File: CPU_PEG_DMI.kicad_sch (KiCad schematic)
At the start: 1 part

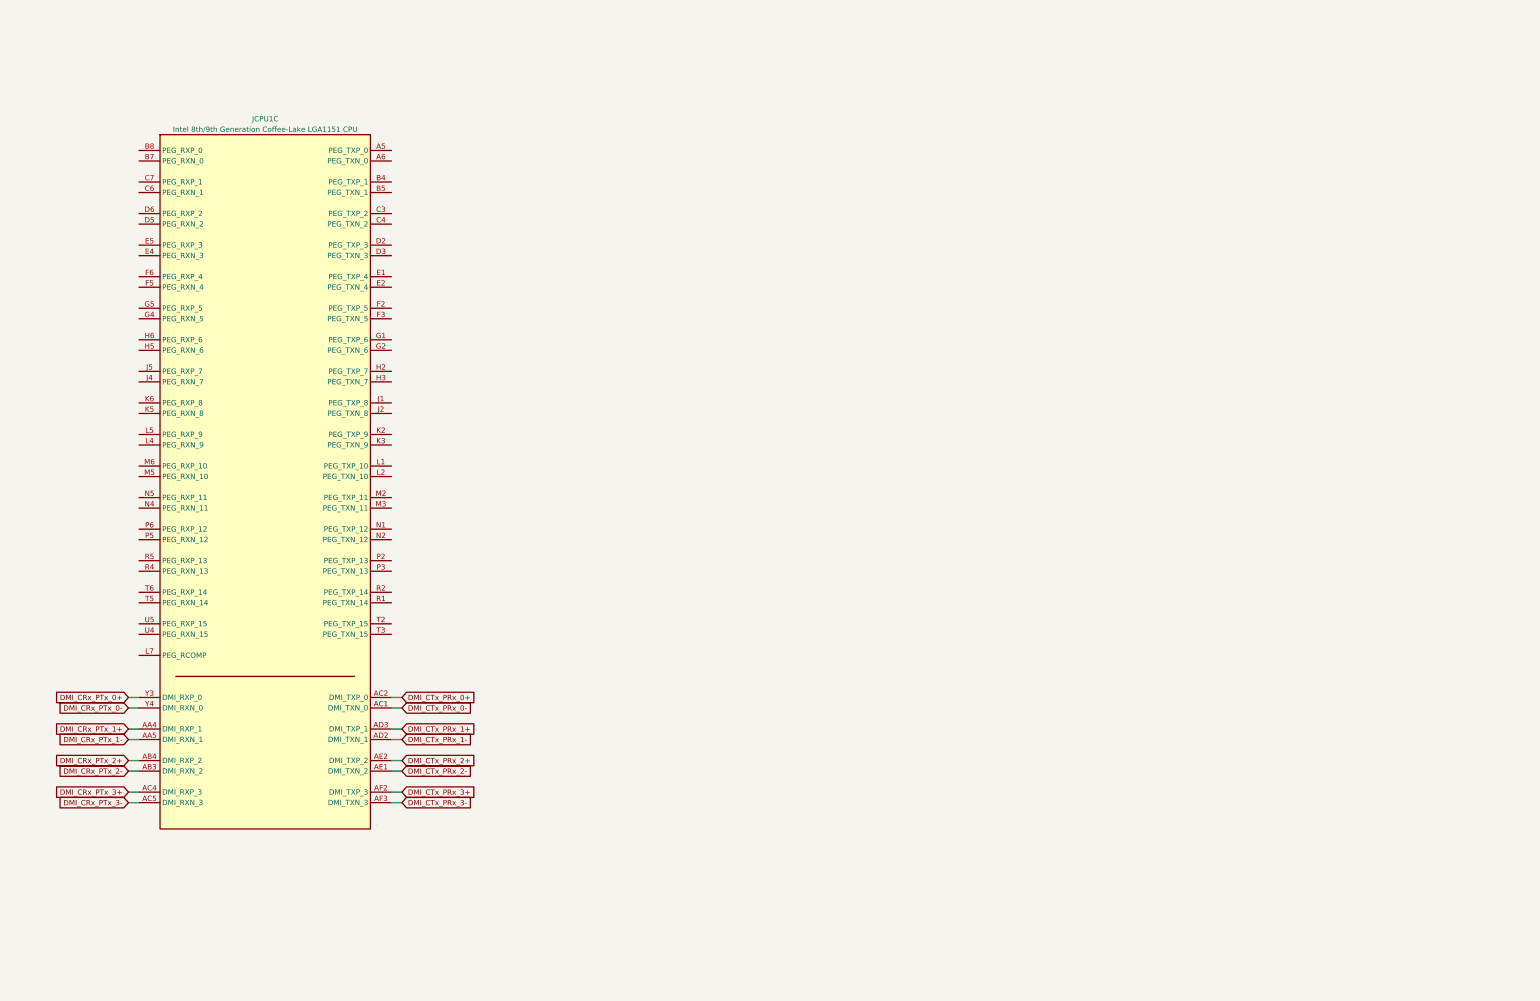
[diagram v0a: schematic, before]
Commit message: Added PCIe x16 slot
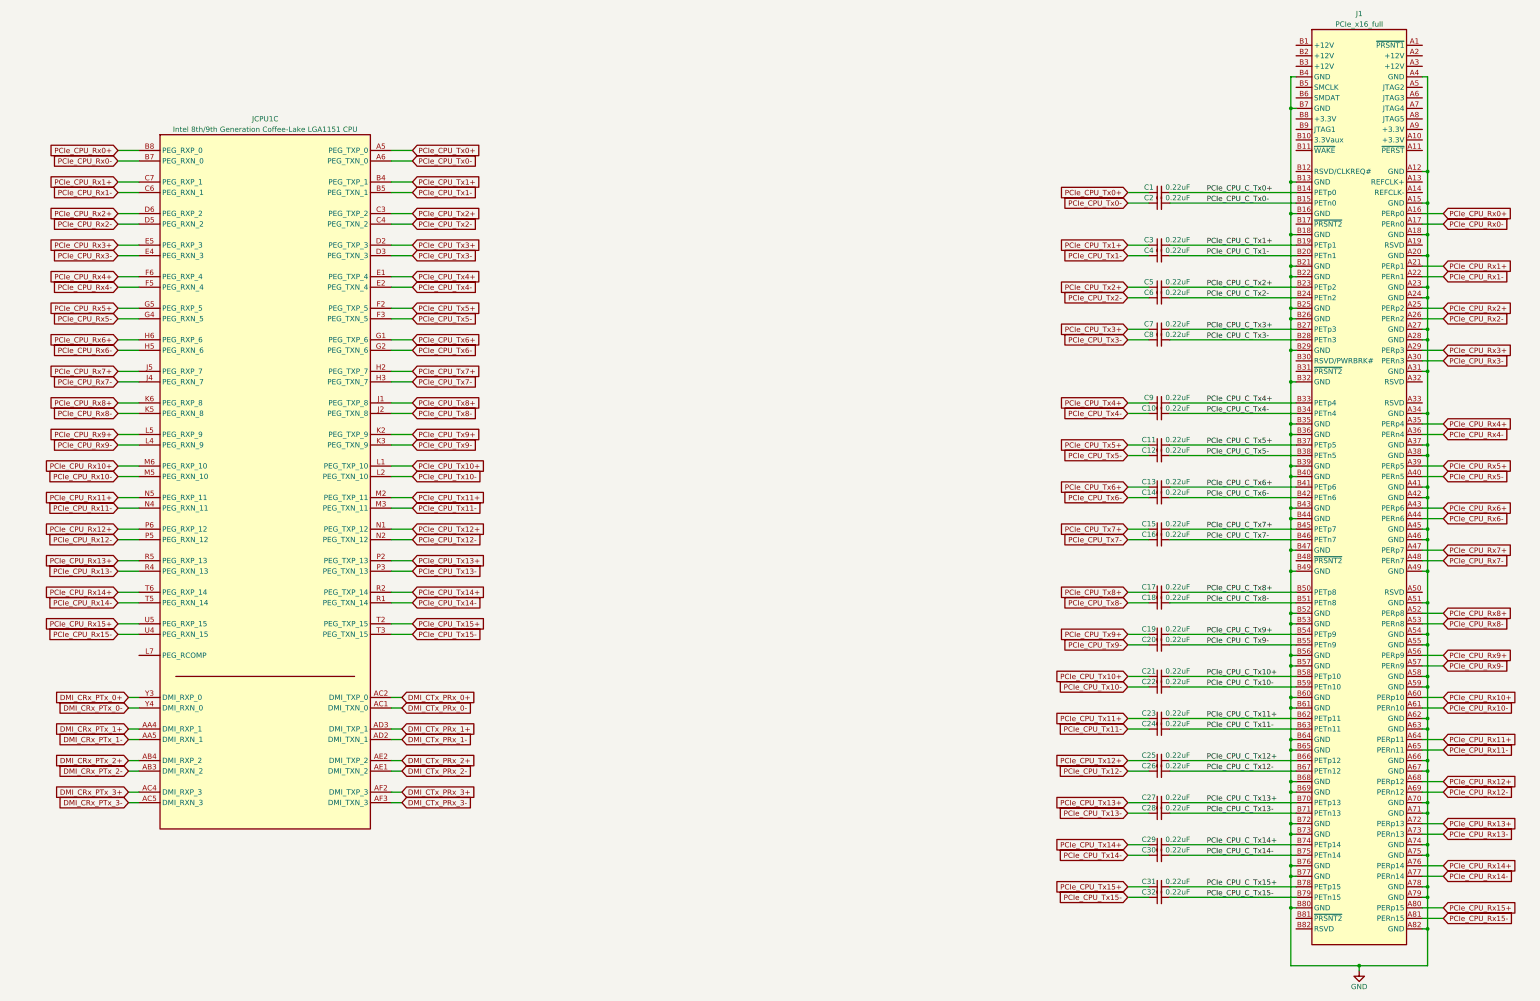
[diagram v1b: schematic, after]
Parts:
- added C1, C10, C11, C12, C13, C14, C15, C16, C17, C18, C19, C2, C20, C21, C22, C23, C24, C25, C26, C27, C28, C29, C3, C30, C31, C32, C4, C5, C6, C7, C8, C9: 0.22uF, Capacitor_SMD:C_0402_1005Metric, symbol Device:C_Small
- added J1: PCIe_x16_full, A-my-stuff:PCIe_x16_tht_smallholes, symbol A-my-stuff:PCIe_x16_full
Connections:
- net PCIe_CPU_Tx0+: now reaches JCPU1.A5 (PEG_TXP_0)
- net PCIe_CPU_Tx0+: now also C1.1
- net PCIe_CPU_Tx0-: now reaches JCPU1.A6 (PEG_TXN_0)
- net PCIe_CPU_Tx0-: now also C2.1
- net PCIe_CPU_Tx1+: now reaches JCPU1.B4 (PEG_TXP_1)
- net PCIe_CPU_Tx1+: now also C3.1
- net PCIe_CPU_Tx1-: now reaches JCPU1.B5 (PEG_TXN_1)
- net PCIe_CPU_Tx1-: now also C4.1
- net PCIe_CPU_Rx0-: now reaches JCPU1.B7 (PEG_RXN_0)
- net PCIe_CPU_Rx0-: now also J1.A17 (PERn0)
- net PCIe_CPU_Rx0+: now reaches JCPU1.B8 (PEG_RXP_0)
- net PCIe_CPU_Rx0+: now also J1.A16 (PERp0)
- net PCIe_CPU_Tx2+: now reaches JCPU1.C3 (PEG_TXP_2)
- net PCIe_CPU_Tx2+: now also C5.1
- net PCIe_CPU_Tx2-: now reaches JCPU1.C4 (PEG_TXN_2)
- net PCIe_CPU_Tx2-: now also C6.1
- net PCIe_CPU_Rx1-: now reaches JCPU1.C6 (PEG_RXN_1)
- net PCIe_CPU_Rx1-: now also J1.A22 (PERn1)
- net PCIe_CPU_Rx1+: now reaches JCPU1.C7 (PEG_RXP_1)
- net PCIe_CPU_Rx1+: now also J1.A21 (PERp1)
- net PCIe_CPU_Tx3+: now reaches JCPU1.D2 (PEG_TXP_3)
- net PCIe_CPU_Tx3+: now also C7.1
- net PCIe_CPU_Tx3-: now reaches JCPU1.D3 (PEG_TXN_3)
- net PCIe_CPU_Tx3-: now also C8.1
- net PCIe_CPU_Rx2-: now reaches JCPU1.D5 (PEG_RXN_2)
- net PCIe_CPU_Rx2-: now also J1.A26 (PERn2)
- net PCIe_CPU_Rx2+: now reaches JCPU1.D6 (PEG_RXP_2)
- net PCIe_CPU_Rx2+: now also J1.A25 (PERp2)
- net PCIe_CPU_Tx4+: now reaches JCPU1.E1 (PEG_TXP_4)
- net PCIe_CPU_Tx4+: now also C9.1
- net PCIe_CPU_Tx4-: now reaches JCPU1.E2 (PEG_TXN_4)
- net PCIe_CPU_Tx4-: now also C10.1
- net PCIe_CPU_Rx3-: now reaches JCPU1.E4 (PEG_RXN_3)
- net PCIe_CPU_Rx3-: now also J1.A30 (PERn3)
- net PCIe_CPU_Rx3+: now reaches JCPU1.E5 (PEG_RXP_3)
- net PCIe_CPU_Rx3+: now also J1.A29 (PERp3)
- net PCIe_CPU_Tx5+: now reaches JCPU1.F2 (PEG_TXP_5)
- net PCIe_CPU_Tx5+: now also C11.1
- net PCIe_CPU_Tx5-: now reaches JCPU1.F3 (PEG_TXN_5)
- net PCIe_CPU_Tx5-: now also C12.1
- net PCIe_CPU_Rx4-: now reaches JCPU1.F5 (PEG_RXN_4)
- net PCIe_CPU_Rx4-: now also J1.A36 (PERn4)
- net PCIe_CPU_Rx4+: now reaches JCPU1.F6 (PEG_RXP_4)
- net PCIe_CPU_Rx4+: now also J1.A35 (PERp4)
- net PCIe_CPU_Tx6+: now reaches JCPU1.G1 (PEG_TXP_6)
- net PCIe_CPU_Tx6+: now also C13.1
- net PCIe_CPU_Tx6-: now reaches JCPU1.G2 (PEG_TXN_6)
- net PCIe_CPU_Tx6-: now also C14.1
- net PCIe_CPU_Rx5-: now reaches JCPU1.G4 (PEG_RXN_5)
- net PCIe_CPU_Rx5-: now also J1.A40 (PERn5)
- net PCIe_CPU_Rx5+: now reaches JCPU1.G5 (PEG_RXP_5)
- net PCIe_CPU_Rx5+: now also J1.A39 (PERp5)
- net PCIe_CPU_Tx7+: now reaches JCPU1.H2 (PEG_TXP_7)
- net PCIe_CPU_Tx7+: now also C15.1
- net PCIe_CPU_Tx7-: now reaches JCPU1.H3 (PEG_TXN_7)
- net PCIe_CPU_Tx7-: now also C16.1
- net PCIe_CPU_Rx6-: now reaches JCPU1.H5 (PEG_RXN_6)
- net PCIe_CPU_Rx6-: now also J1.A44 (PERn6)
- net PCIe_CPU_Rx6+: now reaches JCPU1.H6 (PEG_RXP_6)
- net PCIe_CPU_Rx6+: now also J1.A43 (PERp6)
- net PCIe_CPU_Tx8+: now reaches JCPU1.J1 (PEG_TXP_8)
- net PCIe_CPU_Tx8+: now also C17.1
- net PCIe_CPU_Tx8-: now reaches JCPU1.J2 (PEG_TXN_8)
- net PCIe_CPU_Tx8-: now also C18.1
- net PCIe_CPU_Rx7-: now reaches JCPU1.J4 (PEG_RXN_7)
- net PCIe_CPU_Rx7-: now also J1.A48 (PERn7)
- net PCIe_CPU_Rx7+: now reaches JCPU1.J5 (PEG_RXP_7)
- net PCIe_CPU_Rx7+: now also J1.A47 (PERp7)
- net PCIe_CPU_Tx9+: now reaches JCPU1.K2 (PEG_TXP_9)
- net PCIe_CPU_Tx9+: now also C19.1
- net PCIe_CPU_Tx9-: now reaches JCPU1.K3 (PEG_TXN_9)
- net PCIe_CPU_Tx9-: now also C20.1
- net PCIe_CPU_Rx8-: now reaches JCPU1.K5 (PEG_RXN_8)
- net PCIe_CPU_Rx8-: now also J1.A53 (PERn8)
- net PCIe_CPU_Rx8+: now reaches JCPU1.K6 (PEG_RXP_8)
- net PCIe_CPU_Rx8+: now also J1.A52 (PERp8)
- net PCIe_CPU_Tx10+: now reaches JCPU1.L1 (PEG_TXP_10)
- net PCIe_CPU_Tx10+: now also C21.1
- net PCIe_CPU_Tx10-: now reaches JCPU1.L2 (PEG_TXN_10)
- net PCIe_CPU_Tx10-: now also C22.1
- net PCIe_CPU_Rx9-: now reaches JCPU1.L4 (PEG_RXN_9)
- net PCIe_CPU_Rx9-: now also J1.A57 (PERn9)
- net PCIe_CPU_Rx9+: now reaches JCPU1.L5 (PEG_RXP_9)
- net PCIe_CPU_Rx9+: now also J1.A56 (PERp9)
- net PCIe_CPU_Tx11+: now reaches JCPU1.M2 (PEG_TXP_11)
- net PCIe_CPU_Tx11+: now also C23.1
- net PCIe_CPU_Tx11-: now reaches JCPU1.M3 (PEG_TXN_11)
- net PCIe_CPU_Tx11-: now also C24.1
- net PCIe_CPU_Rx10-: now reaches JCPU1.M5 (PEG_RXN_10)
- net PCIe_CPU_Rx10-: now also J1.A61 (PERn10)
- net PCIe_CPU_Rx10+: now reaches JCPU1.M6 (PEG_RXP_10)
- net PCIe_CPU_Rx10+: now also J1.A60 (PERp10)
- net PCIe_CPU_Tx12+: now reaches JCPU1.N1 (PEG_TXP_12)
- net PCIe_CPU_Tx12+: now also C25.1
- net PCIe_CPU_Tx12-: now reaches JCPU1.N2 (PEG_TXN_12)
- net PCIe_CPU_Tx12-: now also C26.1
- net PCIe_CPU_Rx11-: now reaches JCPU1.N4 (PEG_RXN_11)
- net PCIe_CPU_Rx11-: now also J1.A65 (PERn11)
- net PCIe_CPU_Rx11+: now reaches JCPU1.N5 (PEG_RXP_11)
- net PCIe_CPU_Rx11+: now also J1.A64 (PERp11)
- net PCIe_CPU_Tx13+: now reaches JCPU1.P2 (PEG_TXP_13)
- net PCIe_CPU_Tx13+: now also C27.1
- net PCIe_CPU_Tx13-: now reaches JCPU1.P3 (PEG_TXN_13)
- net PCIe_CPU_Tx13-: now also C28.1
- net PCIe_CPU_Rx12-: now reaches JCPU1.P5 (PEG_RXN_12)
- net PCIe_CPU_Rx12-: now also J1.A69 (PERn12)
- net PCIe_CPU_Rx12+: now reaches JCPU1.P6 (PEG_RXP_12)
- net PCIe_CPU_Rx12+: now also J1.A68 (PERp12)
- net PCIe_CPU_Tx14-: now reaches JCPU1.R1 (PEG_TXN_14)
- net PCIe_CPU_Tx14-: now also C30.1
- net PCIe_CPU_Tx14+: now reaches JCPU1.R2 (PEG_TXP_14)
- net PCIe_CPU_Tx14+: now also C29.1
- net PCIe_CPU_Rx13-: now reaches JCPU1.R4 (PEG_RXN_13)
- net PCIe_CPU_Rx13-: now also J1.A73 (PERn13)
- net PCIe_CPU_Rx13+: now reaches JCPU1.R5 (PEG_RXP_13)
- net PCIe_CPU_Rx13+: now also J1.A72 (PERp13)
- net PCIe_CPU_Tx15+: now reaches JCPU1.T2 (PEG_TXP_15)
- net PCIe_CPU_Tx15+: now also C31.1
- net PCIe_CPU_Tx15-: now reaches JCPU1.T3 (PEG_TXN_15)
- net PCIe_CPU_Tx15-: now also C32.1
- net PCIe_CPU_Rx14-: now reaches JCPU1.T5 (PEG_RXN_14)
- net PCIe_CPU_Rx14-: now also J1.A77 (PERn14)
- net PCIe_CPU_Rx14+: now reaches JCPU1.T6 (PEG_RXP_14)
- net PCIe_CPU_Rx14+: now also J1.A76 (PERp14)
- net PCIe_CPU_Rx15-: now reaches JCPU1.U4 (PEG_RXN_15)
- net PCIe_CPU_Rx15-: now also J1.A81 (PERn15)
- net PCIe_CPU_Rx15+: now reaches JCPU1.U5 (PEG_RXP_15)
- net PCIe_CPU_Rx15+: now also J1.A80 (PERp15)
- new net GND: J1.A12 (GND), J1.A15 (GND), J1.A18 (GND), J1.A20 (GND), J1.A23 (GND), J1.A24 (GND), J1.A27 (GND), J1.A28 (GND), J1.A31 (GND), J1.A34 (GND), J1.A37 (GND), J1.A38 (GND), J1.A4 (GND), J1.A41 (GND), J1.A42 (GND), J1.A45 (GND), J1.A46 (GND), J1.A49 (GND), J1.A51 (GND), J1.A54 (GND), J1.A55 (GND), J1.A58 (GND), J1.A59 (GND), J1.A62 (GND), J1.A63 (GND), J1.A66 (GND), J1.A67 (GND), J1.A70 (GND), J1.A71 (GND), J1.A74 (GND), J1.A75 (GND), J1.A78 (GND), J1.A79 (GND), J1.A82 (GND), J1.B13 (GND), J1.B16 (GND), J1.B18 (GND), J1.B21 (GND), J1.B22 (GND), J1.B25 (GND), J1.B26 (GND), J1.B29 (GND), J1.B32 (GND), J1.B35 (GND), J1.B36 (GND), J1.B39 (GND), J1.B4 (GND), J1.B40 (GND), J1.B43 (GND), J1.B44 (GND), J1.B47 (GND), J1.B49 (GND), J1.B52 (GND), J1.B53 (GND), J1.B56 (GND), J1.B57 (GND), J1.B60 (GND), J1.B61 (GND), J1.B64 (GND), J1.B65 (GND), J1.B68 (GND), J1.B69 (GND), J1.B7 (GND), J1.B72 (GND), J1.B73 (GND), J1.B76 (GND), J1.B77 (GND), J1.B80 (GND)
- new net PCIe_CPU_C_Tx0+: C1.2, J1.B14 (PETp0)
- new net PCIe_CPU_C_Tx0-: C2.2, J1.B15 (PETn0)
- new net PCIe_CPU_C_Tx1+: C3.2, J1.B19 (PETp1)
- new net PCIe_CPU_C_Tx1-: C4.2, J1.B20 (PETn1)
- new net PCIe_CPU_C_Tx10+: C21.2, J1.B58 (PETp10)
- new net PCIe_CPU_C_Tx10-: C22.2, J1.B59 (PETn10)
- new net PCIe_CPU_C_Tx11+: C23.2, J1.B62 (PETp11)
- new net PCIe_CPU_C_Tx11-: C24.2, J1.B63 (PETn11)
- new net PCIe_CPU_C_Tx12+: C25.2, J1.B66 (PETp12)
- new net PCIe_CPU_C_Tx12-: C26.2, J1.B67 (PETn12)
- new net PCIe_CPU_C_Tx13+: C27.2, J1.B70 (PETp13)
- new net PCIe_CPU_C_Tx13-: C28.2, J1.B71 (PETn13)
- new net PCIe_CPU_C_Tx14+: C29.2, J1.B74 (PETp14)
- new net PCIe_CPU_C_Tx14-: C30.2, J1.B75 (PETn14)
- new net PCIe_CPU_C_Tx15+: C31.2, J1.B78 (PETp15)
- new net PCIe_CPU_C_Tx15-: C32.2, J1.B79 (PETn15)
- new net PCIe_CPU_C_Tx2+: C5.2, J1.B23 (PETp2)
- new net PCIe_CPU_C_Tx2-: C6.2, J1.B24 (PETn2)
- new net PCIe_CPU_C_Tx3+: C7.2, J1.B27 (PETp3)
- new net PCIe_CPU_C_Tx3-: C8.2, J1.B28 (PETn3)
- new net PCIe_CPU_C_Tx4+: C9.2, J1.B33 (PETp4)
- new net PCIe_CPU_C_Tx4-: C10.2, J1.B34 (PETn4)
- new net PCIe_CPU_C_Tx5+: C11.2, J1.B37 (PETp5)
- new net PCIe_CPU_C_Tx5-: C12.2, J1.B38 (PETn5)
- new net PCIe_CPU_C_Tx6+: C13.2, J1.B41 (PETp6)
- new net PCIe_CPU_C_Tx6-: C14.2, J1.B42 (PETn6)
- new net PCIe_CPU_C_Tx7+: C15.2, J1.B45 (PETp7)
- new net PCIe_CPU_C_Tx7-: C16.2, J1.B46 (PETn7)
- new net PCIe_CPU_C_Tx8+: C17.2, J1.B50 (PETp8)
- new net PCIe_CPU_C_Tx8-: C18.2, J1.B51 (PETn8)
- new net PCIe_CPU_C_Tx9+: C19.2, J1.B54 (PETp9)
- new net PCIe_CPU_C_Tx9-: C20.2, J1.B55 (PETn9)

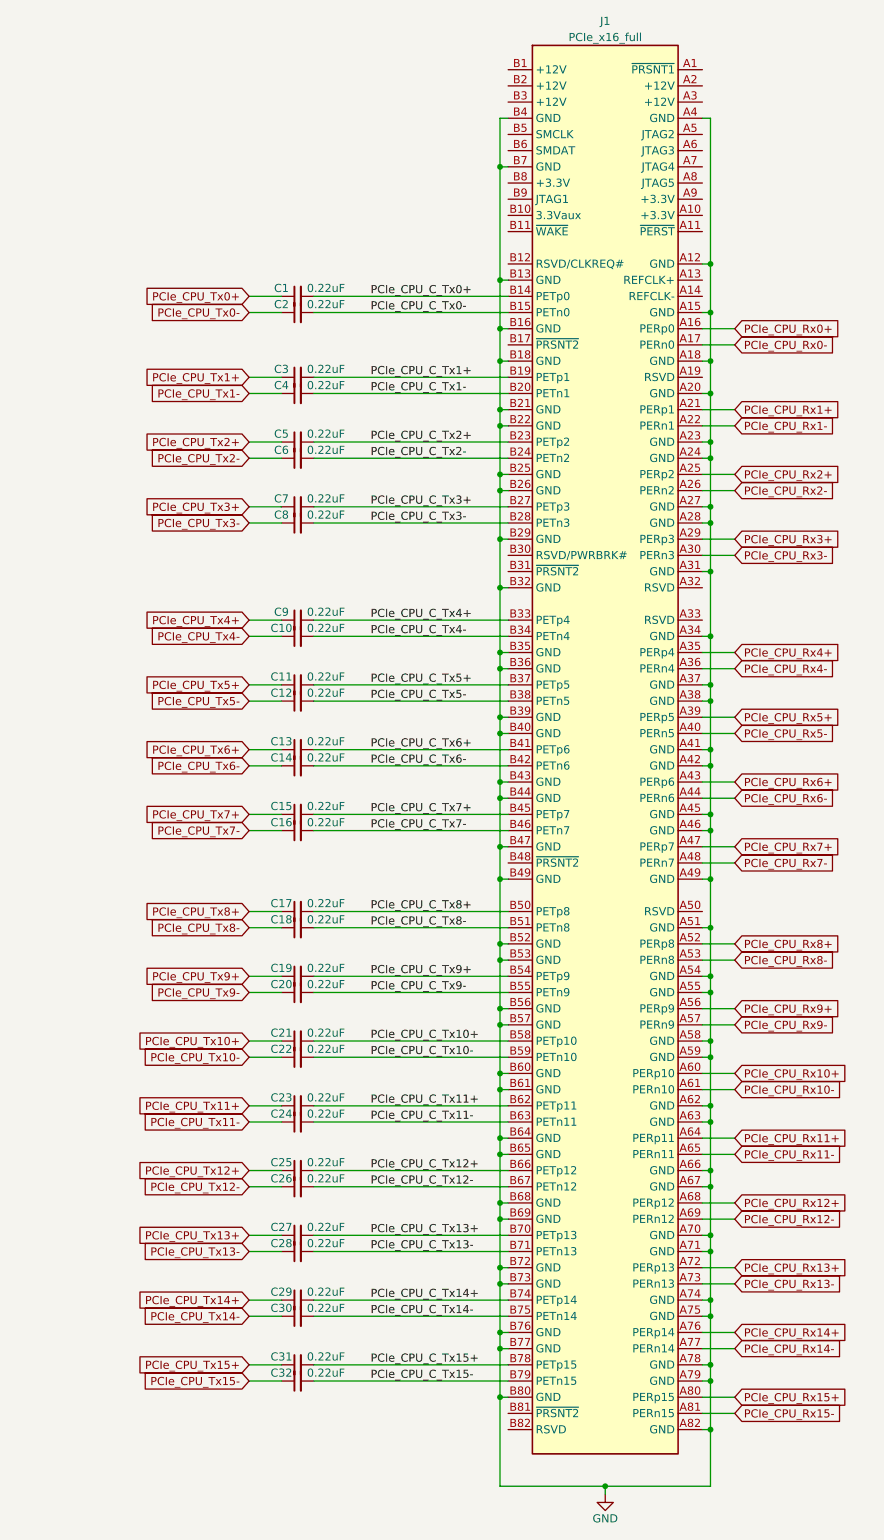
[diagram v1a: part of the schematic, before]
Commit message: Added pcie slot and cpu clocks
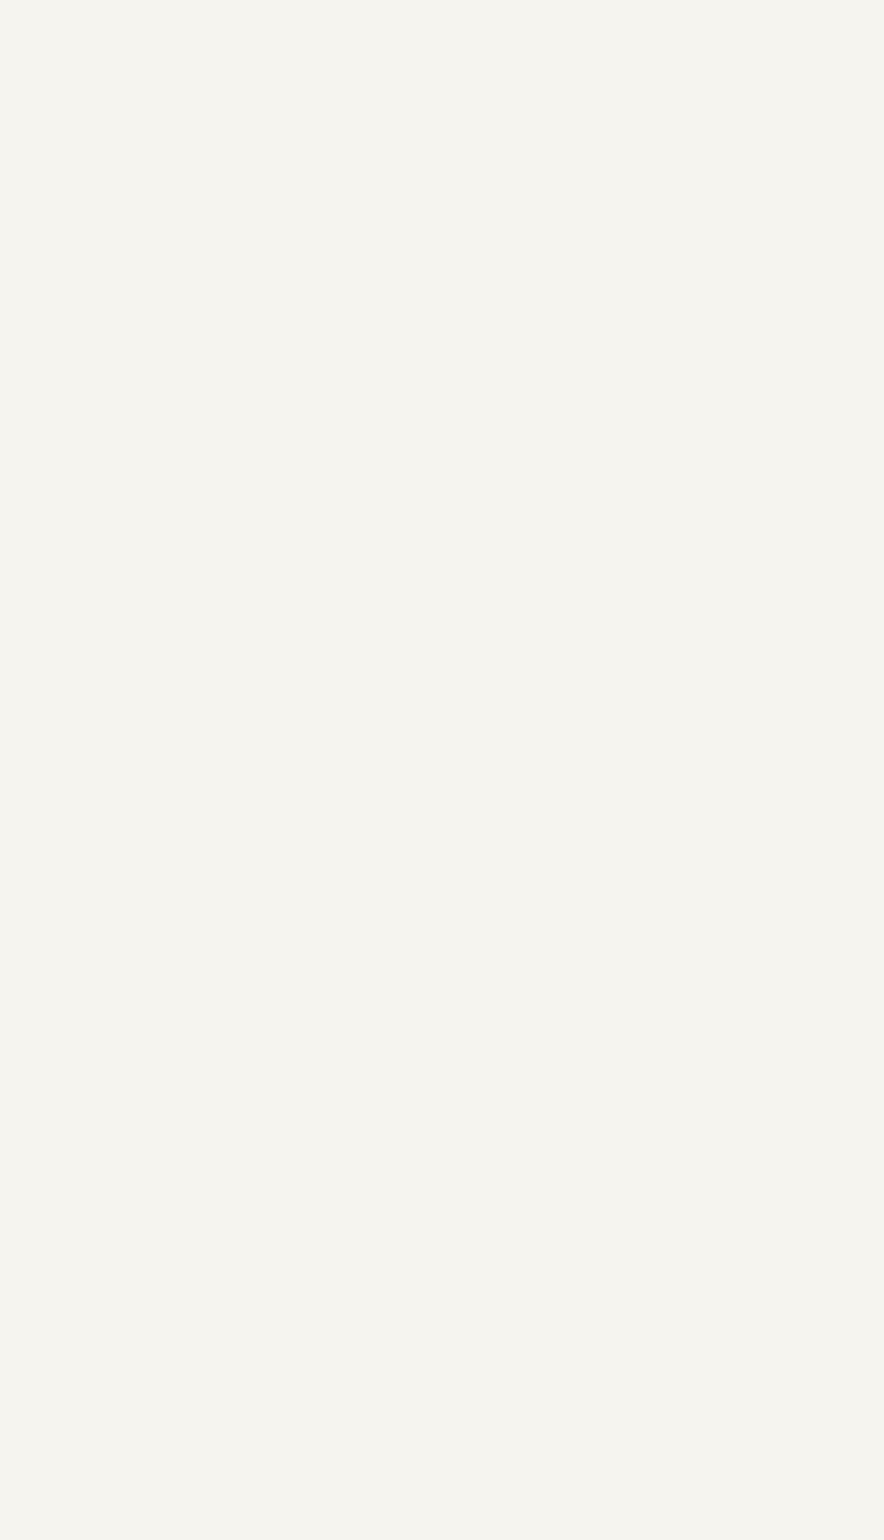
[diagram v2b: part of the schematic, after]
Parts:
- removed C1, C10, C11, C12, C13, C14, C15, C16, C17, C18, C19, C2, C20, C21, C22, C23, C24, C25, C26, C27, C28, C29, C3, C30, C31, C32, C4, C5, C6, C7, C8, C9: 0.22uF, Capacitor_SMD:C_0402_1005Metric, symbol Device:C_Small
- removed J1: PCIe_x16_full, A-my-stuff:PCIe_x16_tht_smallholes, symbol A-my-stuff:PCIe_x16_full

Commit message: partially added eDP + rearranged other display stuff
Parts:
- added R10: 24.9Ω_1%, Resistor_SMD:R_0402_1005Metric, symbol Device:R_Small
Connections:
- net at JCPU1.L7 (PEG_RCOMP): now also R10.2
- new net VCCIO: R10.1
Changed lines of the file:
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@@
+	(wire
+		(pts
+			(xy 76.2 146.05) (xy 86.36 146.05)
+		)
+		(stroke
+			(width 0)
+			(type default)
+		)
+	)
 	(wire
 		(pts
@@
 		)
 	)
+	(wire
+		(pts
+			(xy 58.42 143.51) (xy 58.42 146.05)
+		)
+		(stroke
+			(width 0)
+			(type default)
+		)
+	)
+	(wire
+		(pts
+			(xy 58.42 146.05) (xy 71.12 146.05)
+		)
+		(stroke
+			(width 0)
+			(type default)
+		)
+	)
 	(global_label "DMI_CTx_PRx_2+"
 		(shape input)
@@
 			)
 		)
+	)
+	(symbol
+		(lib_id "Device:R_Small")
+		(at 73.66 146.05 90)
+		(unit 1)
+		(exclude_from_sim no)
+		(in_bom yes)
+		(on_board yes)
+		(dnp no)
+		(property "Reference" "R10"
+			(at 67.31 144.78 90)
+			(effects
+				(font
+					(size 1.27 1.27)
+				)
+				(justify right)
+			)
+		)
+		(property "Value" "24.9Ω_1%"
+			(at 76.2 144.78 90)
+			(effects
+				(font
+					(size 1.27 1.27)
+				)
+				(justify right)
+			)
+		)
+		(property "Footprint" "Resistor_SMD:R_0402_1005Metric"
+			(at 73.66 146.05 0)
+			(effects
+				(font
+					(size 1.27 1.27)
+				)
+				(hide yes)
+			)
+		)
+		(property "Datasheet" "~"
+			(at 73.66 146.05 0)
+			(effects
+				(font
+					(size 1.27 1.27)
+				)
+				(hide yes)
+			)
+		)
+		(property "Description" "Resistor, small symbol"
+			(at 73.66 146.05 0)
+			(effects
+				(font
+					(size 1.27 1.27)
+				)
+				(hide yes)
+			)
+		)
+		(pin "1"
+		)
+		(pin "2"
+		)
+		(instances
+			(project "Stroopwafel-LGA1151-CFL"
+				(path "/4bc771b8-eb19-46d0-8798-27231a7c6e83/061fe2d6-87c2-48c2-90bb-0928700512fc"
+					(reference "R10")
+					(unit 1)
+				)
+			)
+		)
+	)
+	(symbol
+		(lib_id "power:VCC")
+		(at 58.42 143.51 0)
+		(unit 1)
+		(exclude_from_sim no)
+		(in_bom yes)
+		(on_board yes)
+		(dnp no)
+		(property "Reference" "#PWR032"
+			(at 58.42 147.32 0)
+			(effects
+				(font
+					(size 1.27 1.27)
+				)
+				(hide yes)
+			)
+		)
+		(property "Value" "VCCIO"
+			(at 58.42 139.7 0)
+			(effects
+				(font
+					(size 1.27 1.27)
+				)
+			)
+		)
+		(property "Footprint" ""
+			(at 58.42 143.51 0)
+			(effects
+				(font
+					(size 1.27 1.27)
+				)
+				(hide yes)
+			)
+		)
+		(property "Datasheet" ""
+			(at 58.42 143.51 0)
+			(effects
+				(font
+					(size 1.27 1.27)
+				)
+				(hide yes)
+			)
+		)
+		(property "Description" "Power symbol creates a global label with name \"VCC\""
+			(at 58.42 143.51 0)
+			(effects
+				(font
+					(size 1.27 1.27)
+				)
+				(hide yes)
+			)
+		)
+		(pin "1"
+		)
+		(instances
+			(project "Stroopwafel-LGA1151-CFL"
+				(path "/4bc771b8-eb19-46d0-8798-27231a7c6e83/061fe2d6-87c2-48c2-90bb-0928700512fc"
+					(reference "#PWR032")
+					(unit 1)
+				)
+			)
+		)

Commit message: Added LGA1151 socket bracket holes
stolen from another lga1151 footprint that has wrong pin numbers....
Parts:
- JCPU1: footprint A-my-stuff:LGA-1151_L47.1-W42.5-P0.91_PE115127-4041-01H -> A-my-stuff:LGA1151_TE-2287402-1
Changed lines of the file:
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@@
 			)
 		)
-		(property "Footprint" "A-my-stuff:LGA-1151_L47.1-W42.5-P0.91_PE115127-4041-01H"
+		(property "Footprint" "A-my-stuff:LGA1151_TE-2287402-1"
 			(at 116.84 226.06 0)
 			(effects

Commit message: Added CPU CFG resistors
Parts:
- JCPU1: footprint A-my-stuff:LGA1151_TE-2287402-1 -> A-my-stuff:LGA-1151_L47.1-W42.5-P0.91_PE115127-4041-01H
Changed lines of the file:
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@@
 			)
 		)
-		(property "Footprint" "A-my-stuff:LGA1151_TE-2287402-1"
+		(property "Footprint" "A-my-stuff:LGA-1151_L47.1-W42.5-P0.91_PE115127-4041-01H"
 			(at 116.84 226.06 0)
 			(effects
